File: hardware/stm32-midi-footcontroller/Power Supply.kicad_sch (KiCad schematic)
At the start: 18 parts, among them J1 Barrel_Jack, Q1 DMP6023LE, U1 MCP16301, U2 AMS1117-3.3

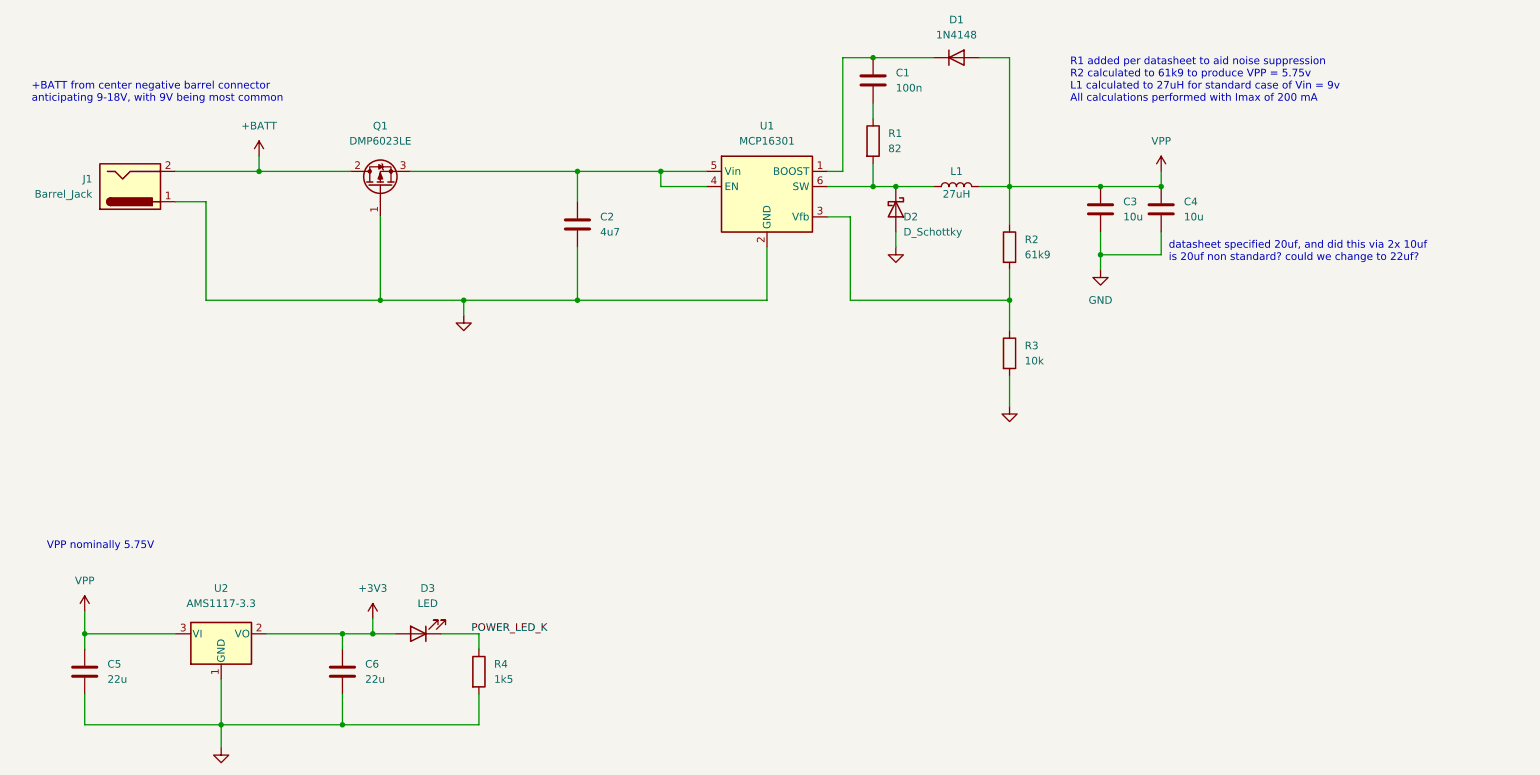
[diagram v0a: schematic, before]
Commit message: begin work on MCU schematic page
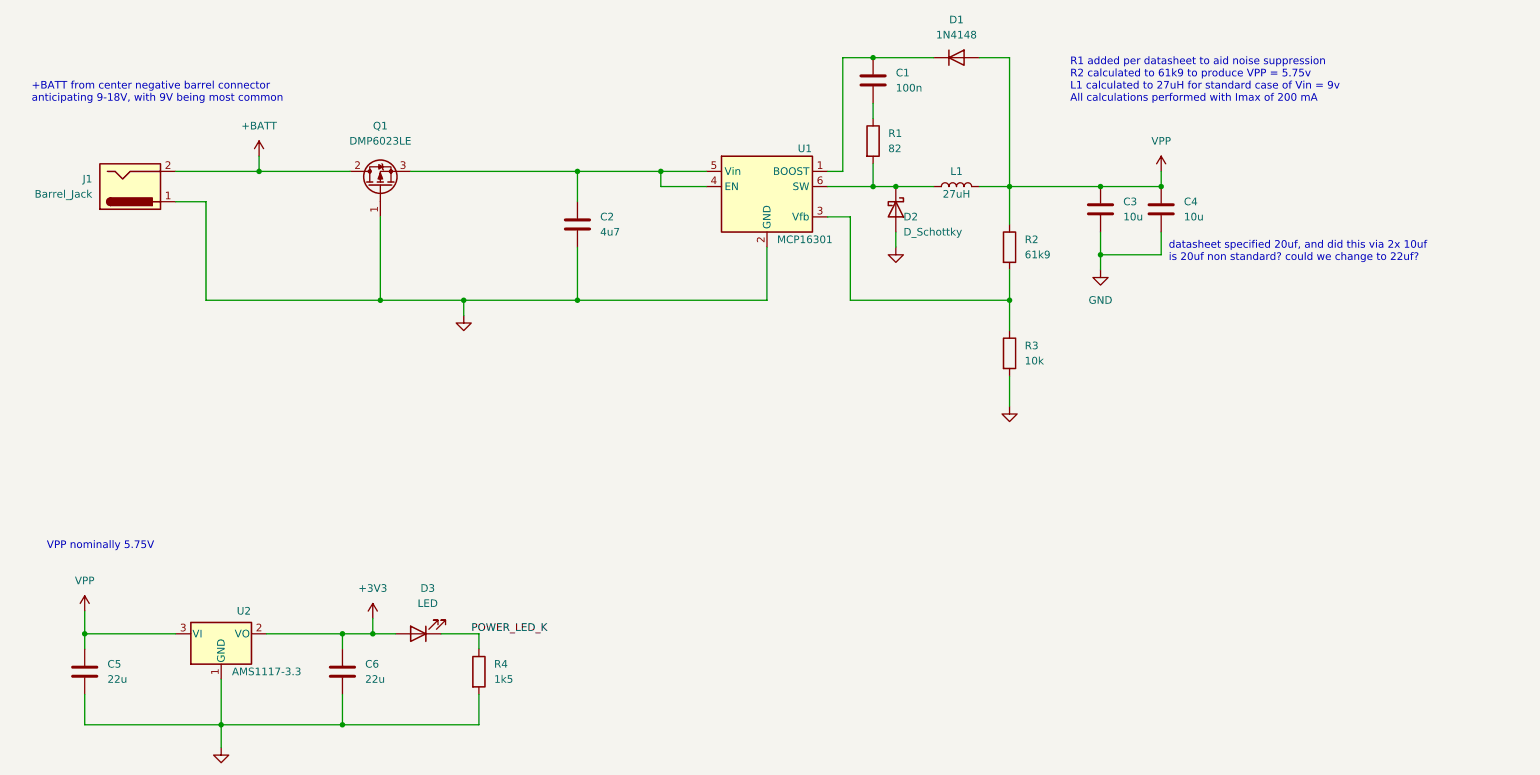
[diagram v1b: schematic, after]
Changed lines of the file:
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@@
   )
   (symbol (lib_id "Regulator_Switching:MCP16301") (at 147.32 53.34 0) (unit 1)
-    (in_bom yes) (on_board yes) (fields_autoplaced)
-    (property "Reference" "U1" (id 0) (at 147.32 43.18 0))
-    (property "Value" "MCP16301" (id 1) (at 147.32 45.72 0))
+    (in_bom yes) (on_board yes)
+    (property "Reference" "U1" (id 0) (at 153.67 46.99 0))
+    (property "Value" "MCP16301" (id 1) (at 153.67 62.23 0))
     (property "Footprint" "Package_TO_SOT_SMD:SOT-23-6" (id 2) (at 148.59 62.23 0)
       (effects (font (size 1.27 1.27)) (justify left) hide)
@@
   )
   (symbol (lib_id "Regulator_Linear:AMS1117-3.3") (at 55.88 128.27 0) (unit 1)
-    (in_bom yes) (on_board yes) (fields_autoplaced)
-    (property "Reference" "U2" (id 0) (at 55.88 120.65 0))
-    (property "Value" "AMS1117-3.3" (id 1) (at 55.88 123.19 0))
+    (in_bom yes) (on_board yes)
+    (property "Reference" "U2" (id 0) (at 59.69 124.46 0))
+    (property "Value" "AMS1117-3.3" (id 1) (at 63.5 134.62 0))
     (property "Footprint" "Package_TO_SOT_SMD:SOT-223-3_TabPin2" (id 2) (at 55.88 123.19 0)
       (effects (font (size 1.27 1.27)) hide)

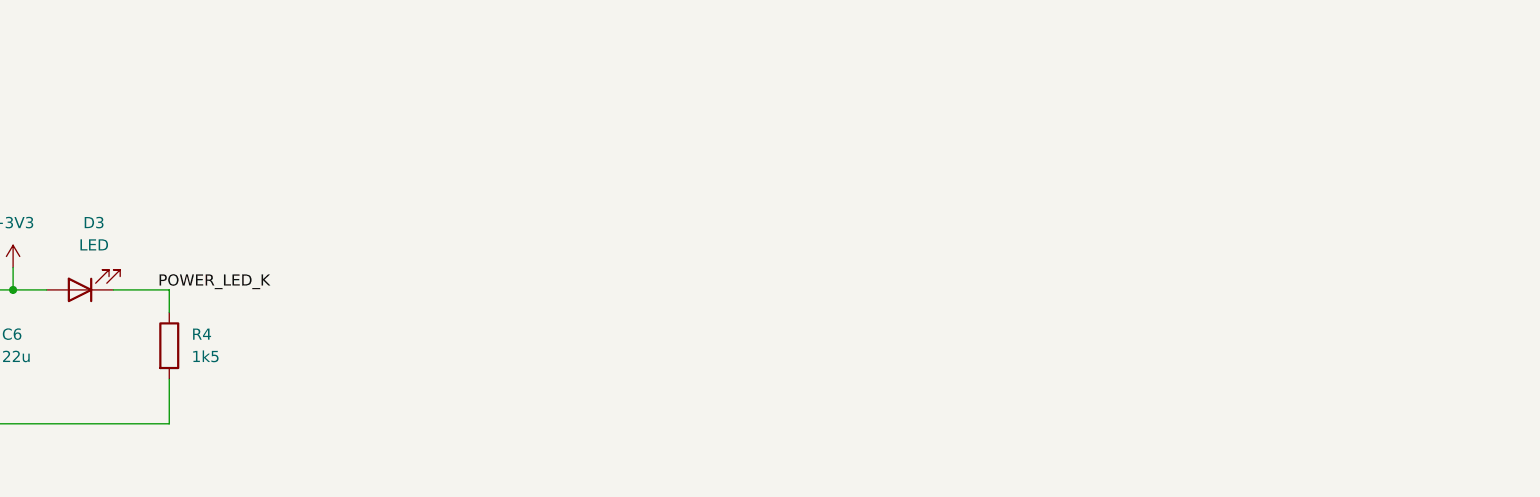
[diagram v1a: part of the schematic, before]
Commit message: add 5v rail, fill out usb host, add usb vout smart fet to library
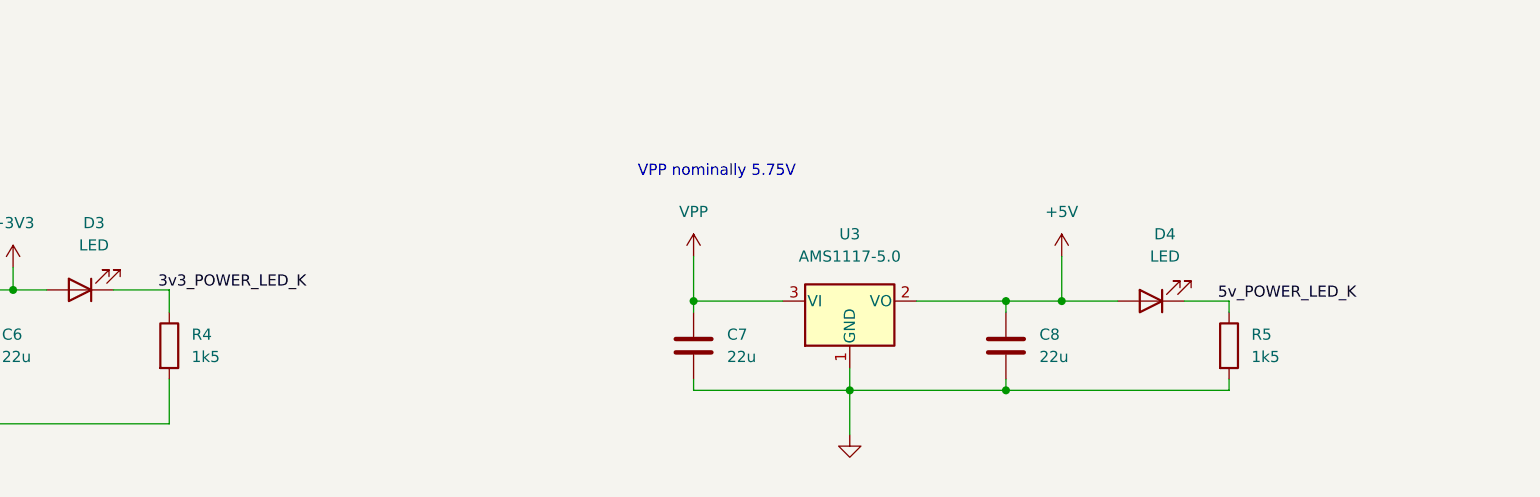
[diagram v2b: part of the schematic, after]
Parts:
- added C7, C8: 22u, symbol Device:C
- added D4: LED, symbol Device:LED
- added R5: 1k5, symbol Device:R
- added U3: AMS1117-5.0, Package_TO_SOT_SMD:SOT-223-3_TabPin2, symbol Regulator_Linear:AMS1117-5.0
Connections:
- net GND: now also C7.2, C8.2, R5.2, U3.1 (GND)
- net VPP: now also C7.1, U3.3 (VI)
- net POWER_LED_K renamed 3v3_POWER_LED_K
- new net +5V: C8.1, D4.2 (A), U3.2 (VO)
- new net 5v_POWER_LED_K: D4.1 (K), R5.1
